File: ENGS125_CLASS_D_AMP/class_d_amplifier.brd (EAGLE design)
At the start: 89.8 x 64.8 mm, 31 parts, among them J1 BANANA_JACK_CT3151, J2 BANANA_JACK_CT3151, J3 BANANA_JACK_CT3151, J4 BANANA_JACK_CT3151, J5 BANANA_JACK_CT3151, J6 BANANA_JACK_CT3151, M1 BSC050NE2LSATMA1, M2 BSC050NE2LSATMA1, U1 LTC6992TSOT-23, U2 LTC4442

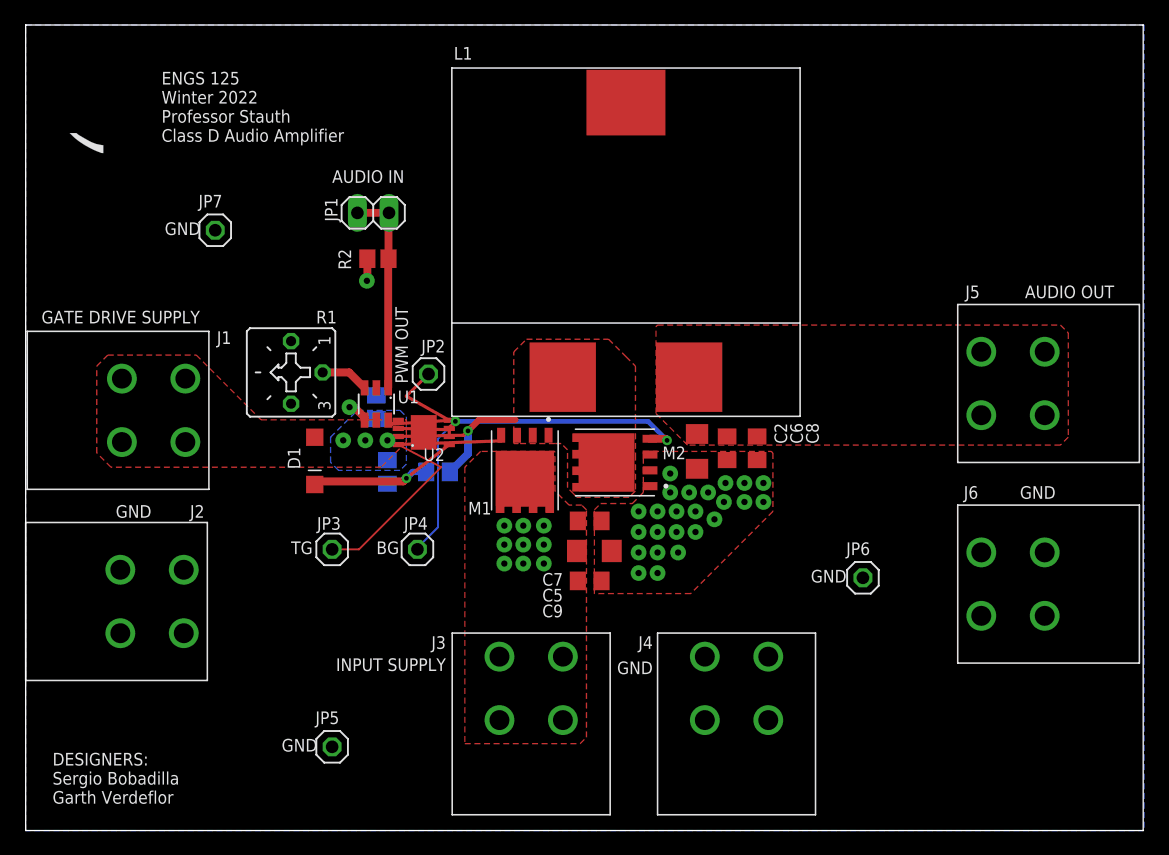
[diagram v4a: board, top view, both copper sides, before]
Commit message: Added converter specs to silkscreen
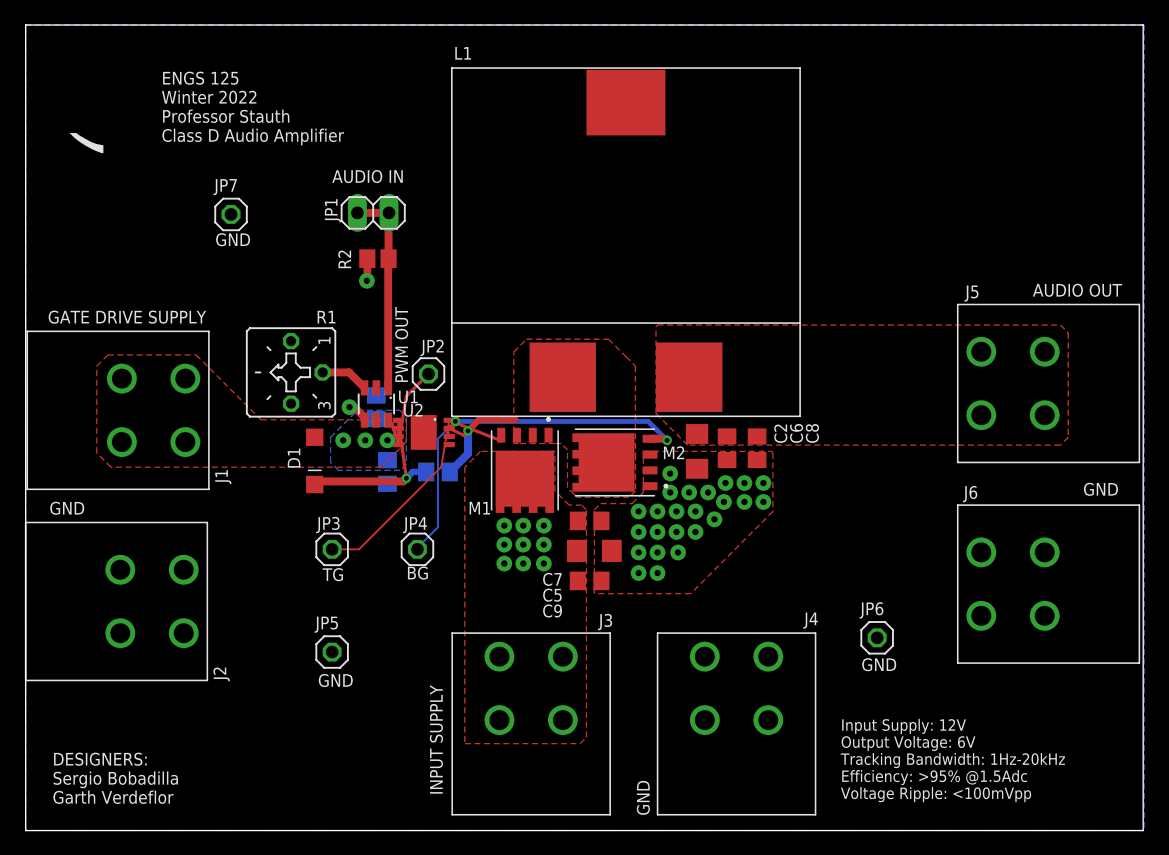
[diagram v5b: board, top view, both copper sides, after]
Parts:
- U2: value LTC4442 -> (none)
- moved JP5 7.62 mm to (24.6, 14.4)
- moved JP6 4.96 mm to (68.5, 15.5)
- moved JP7 1.80 mm to (16.5, 49.5)
- turned U2 to 270 degrees
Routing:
- net VSW: track 13.8 -> 9.86 mm
- net TG: track 24.1 -> 20.3 mm
- net BG: track 35.5 -> 32.1 mm
- net VPWM: track 11.5 -> 8.63 mm
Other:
- board text added: "Input Supply: 12V Output Voltage: 6V Tracking Bandwidth: 1Hz-20kHz Efficiency: >95% @1.5Adc Voltage Ripple: <100mVpp"

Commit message: Rerouted gate driver IC for different component footprint
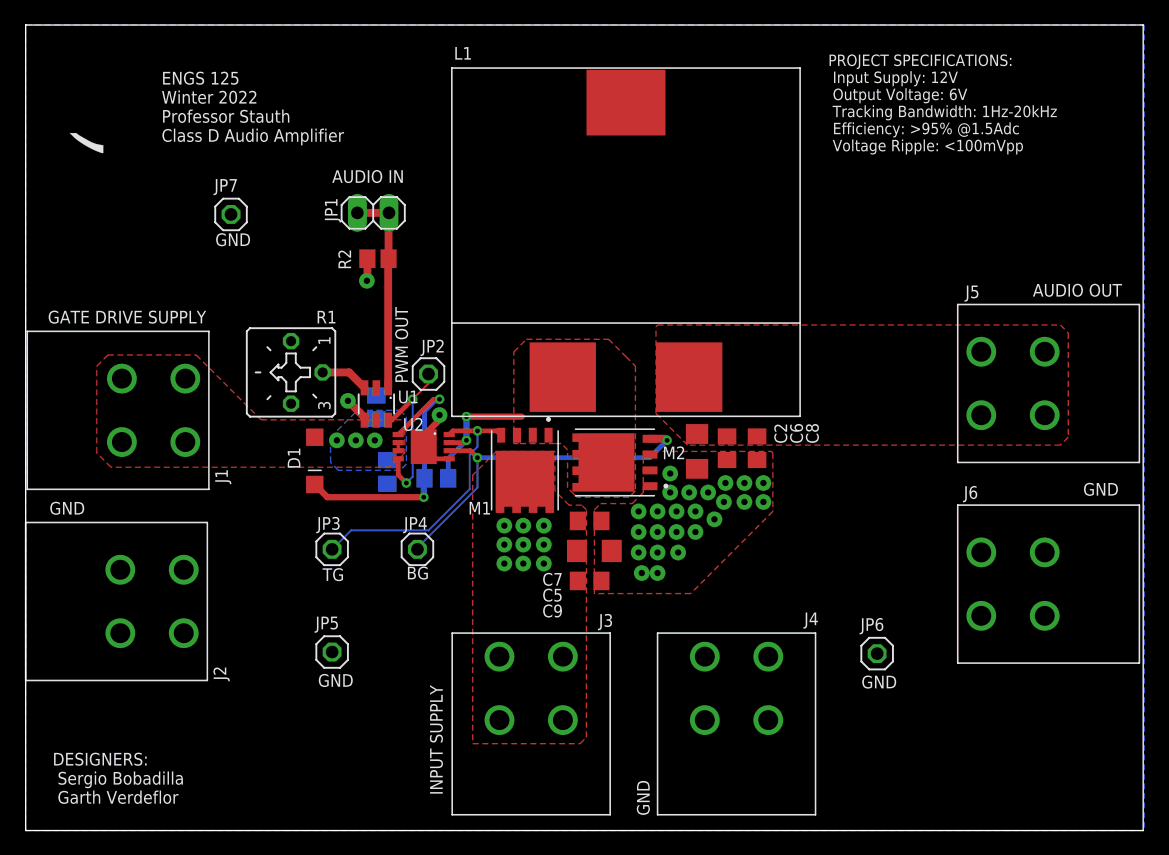
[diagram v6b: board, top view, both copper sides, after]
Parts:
- moved JP6 1.27 mm to (68.5, 14.2)
- moved U2 1.14 mm to (32.0, 30.9)
- moved C1 0.52 mm to (33.0, 28.3)
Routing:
- net N$2: track 14.1 -> 22.2 mm, vias 1 -> 2
- net GND: track 3.56 -> 9.42 mm, vias 26 -> 27
- net VPWM: track 8.63 -> 14.4 mm, vias 0 -> 2
- net BG: track 32.1 -> 29.1 mm
- net TG: track 20.3 -> 22.5 mm, vias 0 -> 1
- net VSW: track 9.86 -> 11.5 mm, vias 1 -> 2
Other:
- board text added: "PROJECT SPECIFICATIONS: Input Supply: 12V Output Voltage: 6V Tracking Bandwidth: 1Hz-20kHz Efficiency: >95% @1.5Adc Voltage Ripple: <100mVpp"
- board text removed: "Input Supply: 12V Output Voltage: 6V Tracking Bandwidth: 1Hz-20kHz Efficiency: >95% @1.5Adc Voltage Ripple: <100mVpp"

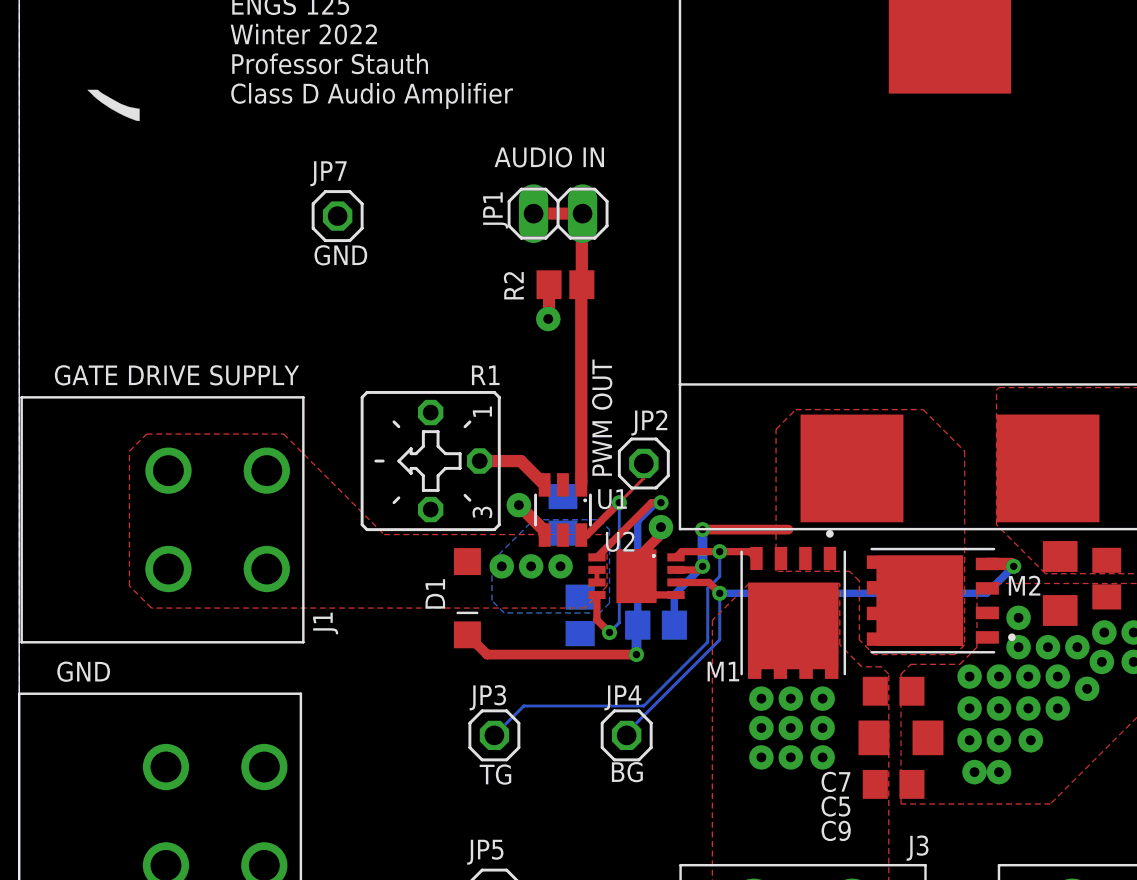
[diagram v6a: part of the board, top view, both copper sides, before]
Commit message: Reorganized gate drive layout to minimize signal length and GND plane cutouts.
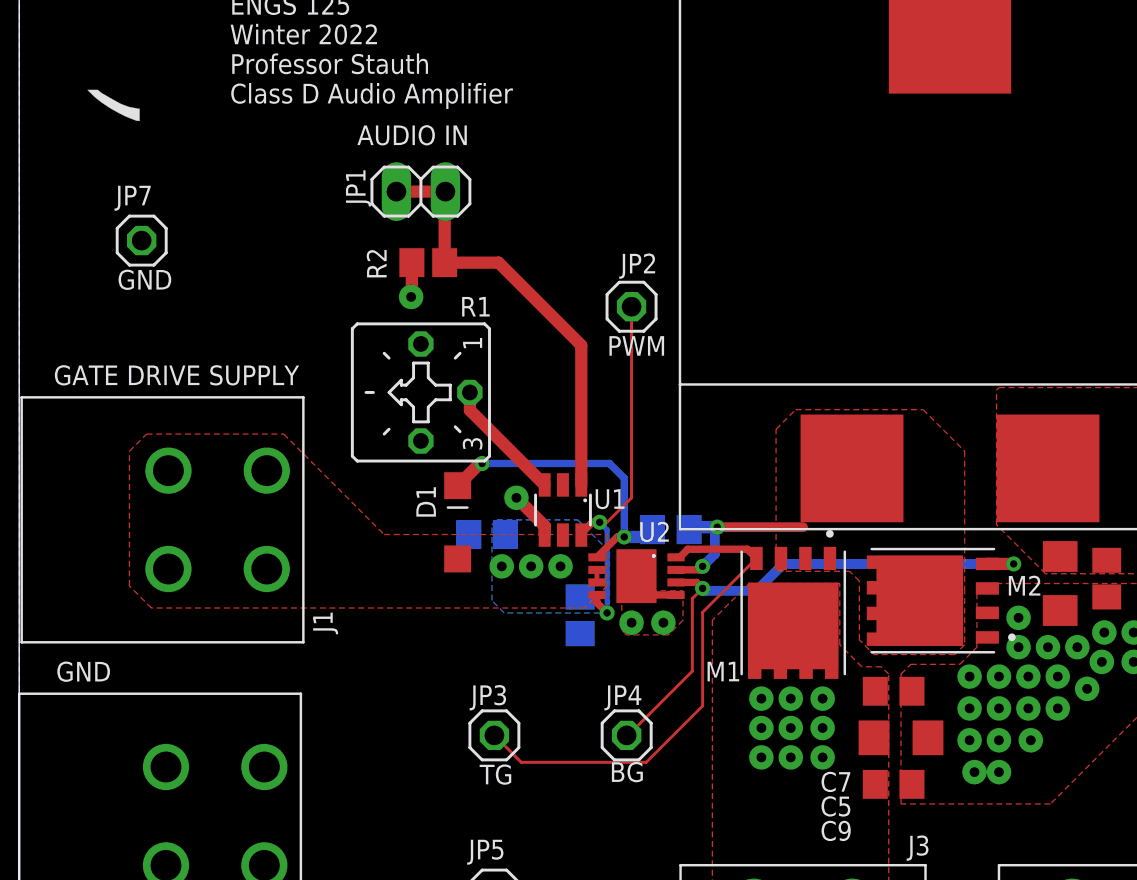
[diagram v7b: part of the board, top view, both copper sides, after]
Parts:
- moved JP7 10.2 mm to (6.35, 48.3)
- moved JP2 8.15 mm to (31.8, 44.8)
- moved JP1 7.20 mm to (20.8, 50.8)
- moved R2 7.20 mm to (21.2, 47.1)
- moved C1 5.01 mm to (33.8, 33.3)
- moved C3 4.07 mm to (24.3, 33.0), turned to 0 degrees
- moved D1 3.97 mm to (22.7, 33.7), turned to 90 degrees
- moved R1 3.59 mm to (20.8, 40.4)
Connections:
- net N$2 renamed BOOST
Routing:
- net BOOST: track 22.2 -> 15.9 mm
- net N$4: track 16.6 -> 22.3 mm
- net VPWM: track 14.4 -> 19.4 mm
- net TG: track 22.5 -> 25.9 mm, vias 1 -> 0
- net GND: track 9.42 -> 6.79 mm, vias 27 -> 28
- net N$1: track 3.88 -> 6.40 mm
- net VSW: track 11.5 -> 9.76 mm
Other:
- board text added: "PWM"
- board text removed: "PWM OUT"

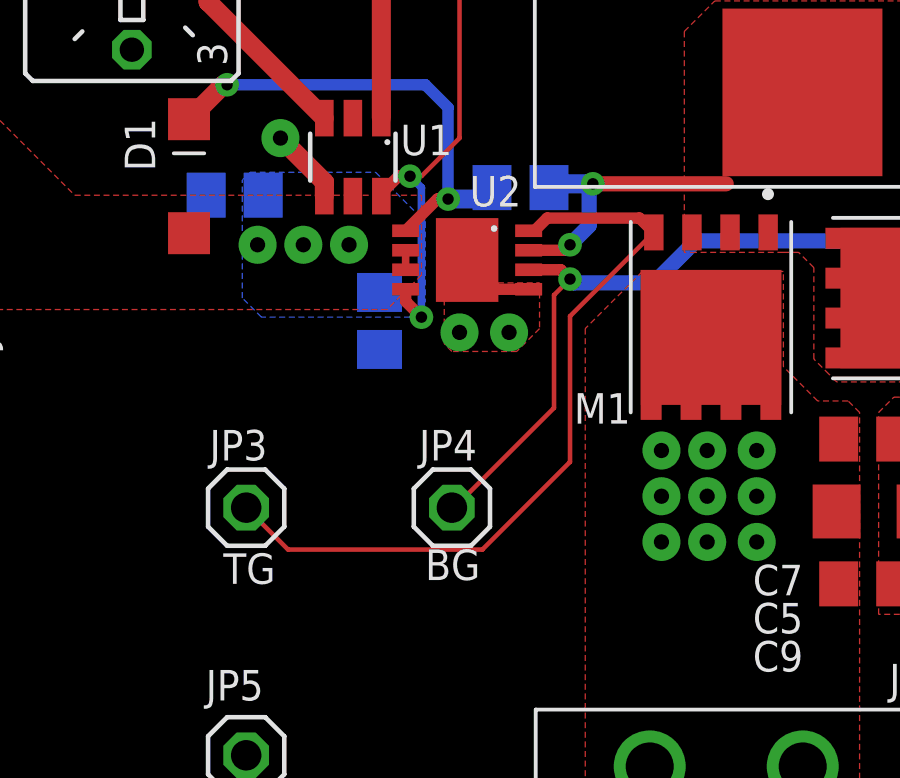
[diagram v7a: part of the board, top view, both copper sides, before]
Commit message: Added in NEW library with updated LTC4442 footprint.
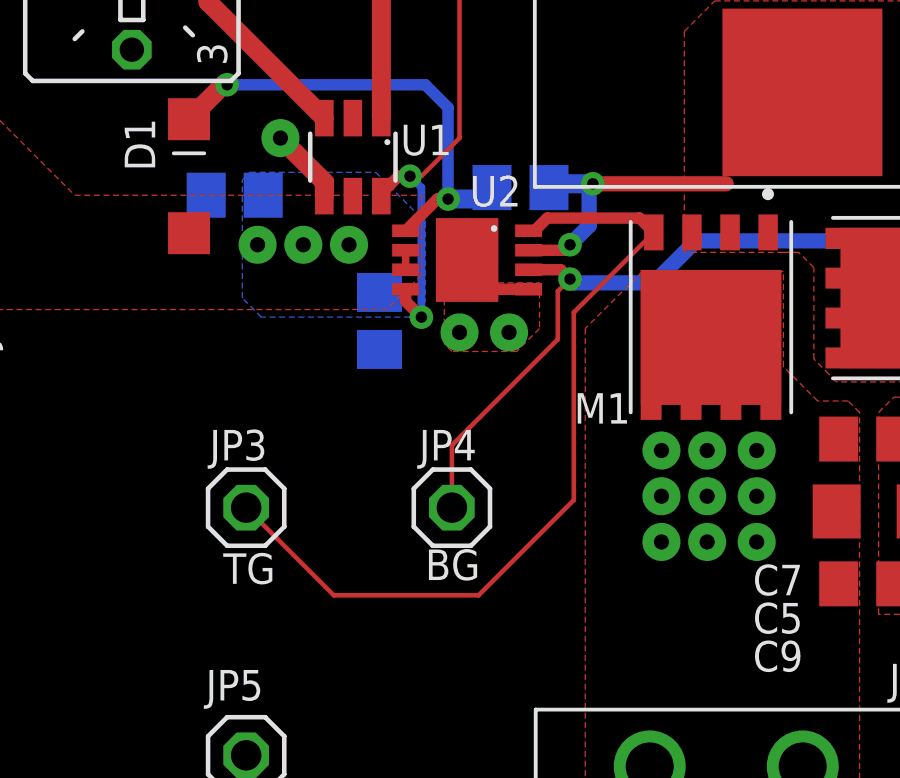
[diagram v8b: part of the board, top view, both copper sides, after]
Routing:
- net TG: track 25.9 -> 28.0 mm
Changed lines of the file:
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@@
 <wire x1="32.979" y1="29.886" x2="32.004" y2="30.861" width="0.381" layer="1"/>
 <via x="31.75" y="28.448" extent="1-16" drill="0.508" diameter="1.27"/>
+<wire x1="32.004" y1="30.861" x2="31.75" y2="30.607" width="0.508" layer="1"/>
 <polygon width="0.127" layer="1" thermals="no">
 <vertex x="31.242" y="28.067"/>
@@
 <wire x1="29.954" y1="31.836" x2="31.011" y2="32.893" width="0.381" layer="1"/>
 <wire x1="31.011" y1="32.893" x2="31.369" y2="32.893" width="0.381" layer="1"/>
+<wire x1="32.766" y1="33.208" x2="32.832" y2="33.274" width="0.508" layer="16"/>
 <wire x1="32.832" y1="33.274" x2="32.451" y2="32.893" width="0.635" layer="16"/>
 <wire x1="32.451" y1="32.893" x2="31.369" y2="32.893" width="0.635" layer="16"/>
@@
 <wire x1="35.433" y1="30.226" x2="35.123" y2="30.536" width="0.381" layer="1"/>
 <wire x1="35.123" y1="30.536" x2="34.054" y2="30.536" width="0.381" layer="1"/>
-<wire x1="34.8996" y1="29.6926" x2="35.433" y2="30.226" width="0.1524" layer="1"/>
-<wire x1="34.8996" y1="25.93128125" x2="34.8996" y2="29.6926" width="0.1524" layer="1"/>
-<wire x1="34.8996" y1="25.93128125" x2="31.57431875" y2="22.606" width="0.1524" layer="1"/>
-<wire x1="31.496" y1="22.606" x2="31.57431875" y2="22.606" width="0.1524" layer="1"/>
+<wire x1="35.0266" y1="29.8196" x2="35.433" y2="30.226" width="0.1524" layer="1"/>
+<wire x1="35.0266" y1="28.21728125" x2="35.0266" y2="29.8196" width="0.1524" layer="1"/>
+<wire x1="31.496" y1="22.606" x2="31.496" y2="24.68668125" width="0.1524" layer="1"/>
+<wire x1="31.496" y1="24.68668125" x2="35.0266" y2="28.21728125" width="0.1524" layer="1"/>
 </signal>
 <signal name="TG">
@@
 <wire x1="34.671" y1="32.258" x2="37.75" y2="32.258" width="0.381" layer="1"/>
 <wire x1="37.75" y1="32.258" x2="38.227" y2="31.781" width="0.381" layer="1"/>
-<wire x1="38.227" y1="31.781" x2="35.433" y2="28.987" width="0.1524" layer="1"/>
-<wire x1="35.433" y1="24.13" x2="32.512" y2="21.209" width="0.1524" layer="1"/>
-<wire x1="32.512" y1="21.209" x2="26.035" y2="21.209" width="0.1524" layer="1"/>
-<wire x1="26.035" y1="21.209" x2="24.638" y2="22.606" width="0.1524" layer="1"/>
-<wire x1="35.433" y1="28.987" x2="35.433" y2="24.13" width="0.1524" layer="1"/>
+<wire x1="38.227" y1="31.781" x2="35.56" y2="29.114" width="0.1524" layer="1"/>
+<wire x1="35.56" y1="22.86" x2="32.385" y2="19.685" width="0.1524" layer="1"/>
+<wire x1="32.385" y1="19.685" x2="27.559" y2="19.685" width="0.1524" layer="1"/>
+<wire x1="27.559" y1="19.685" x2="24.638" y2="22.606" width="0.1524" layer="1"/>
+<wire x1="35.56" y1="29.114" x2="35.56" y2="22.86" width="0.1524" layer="1"/>
 </signal>
 <signal name="N$3">
